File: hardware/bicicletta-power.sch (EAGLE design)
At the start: 24 parts, among them IC1 LM5017, IC2 LM1117-3.3

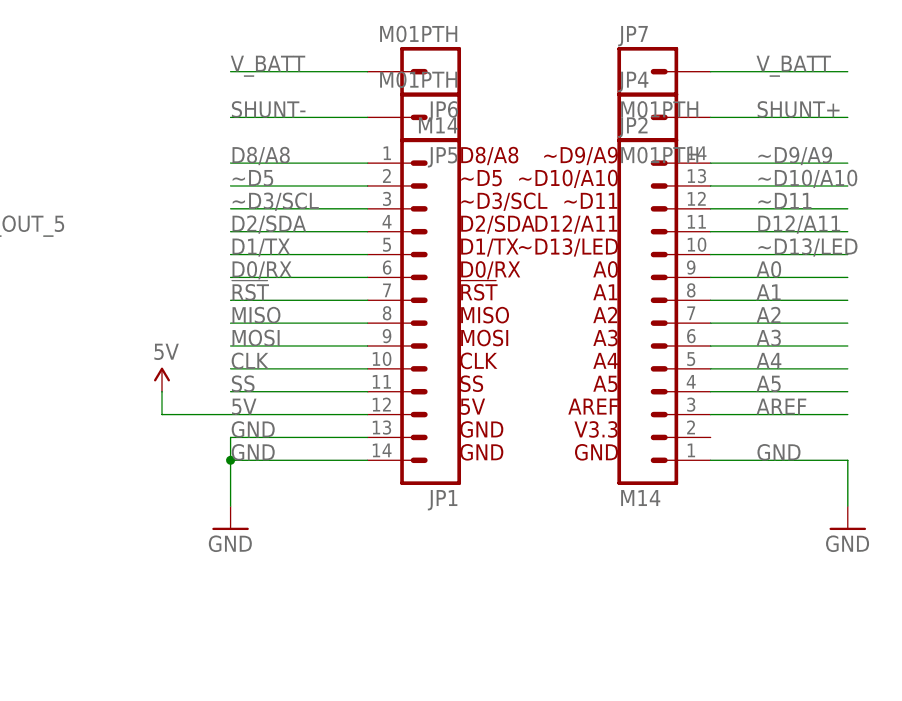
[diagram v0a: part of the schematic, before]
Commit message: Updated to include actual component for the BLEND MICRO
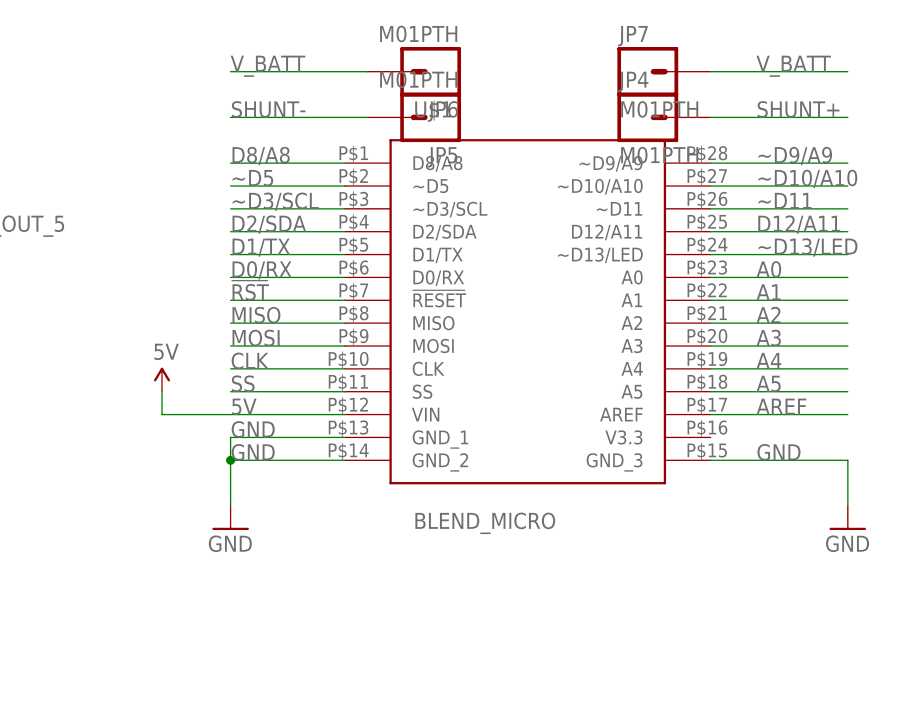
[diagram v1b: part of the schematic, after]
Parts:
- removed JP1, JP2: M14, SparkFun-Connectors:M14
- added U$1: BLEND_MICRO, Railstars:BLEND_MICRO
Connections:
- net !RST: now also U$1.!RESET; no longer JP1.7
- net 5V: now also U$1.VIN; no longer JP1.12
- net A0: now also U$1.A0; no longer JP2.9
- net A1: now also U$1.A1; no longer JP2.8
- net A2: now also U$1.A2; no longer JP2.7
- net A3: now also U$1.A3; no longer JP2.6
- net A4: now also U$1.A4; no longer JP2.5
- net A5: now also U$1.A5; no longer JP2.4
- net AREF: now also U$1.AREF; no longer JP2.3
- net CLK: now also U$1.CLK; no longer JP1.10
- net D0/RX: now also U$1.D0/RX; no longer JP1.6
- net D1/TX: now also U$1.D1/TX; no longer JP1.5
- net D12/A11: now also U$1.D12/A11; no longer JP2.11
- net D2/SDA: now also U$1.D2/SDA; no longer JP1.4
- net D8/A8: now also U$1.D8/A8; no longer JP1.1
- net GND: now also U$1.GND_1, U$1.GND_2, U$1.GND_3; no longer JP1.13, JP1.14, JP2.1
- net MISO: now also U$1.MISO; no longer JP1.8
- net MOSI: now also U$1.MOSI; no longer JP1.9
- net SHUNT-: now also JP5.1
- net SS: now also U$1.SS; no longer JP1.11
- net ~D10/A10: now also U$1.~D10/A10; no longer JP2.13
- net ~D11: now also U$1.~D11; no longer JP2.12
- net ~D13/LED: now also U$1.~D13/LED; no longer JP2.10
- net ~D3/SCL: now also U$1.~D3/SCL; no longer JP1.3
- net ~D5: now also U$1.~D5; no longer JP1.2
- net ~D9/A9: now also U$1.~D9/A9; no longer JP2.14
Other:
- note removed: "!RST"
- note removed: "5V"
- note removed: "A0"
- note removed: "A1"
- note removed: "A2"
- note removed: "A3"
- note removed: "A4"
- note removed: "A5"
- note removed: "AREF"
- note removed: "CLK"
- note removed: "D0/RX"
- note removed: "D1/TX"
- note removed: "D12/A11"
- note removed: "D2/SDA"
- note removed: "D8/A8"
- note removed: "GND"
- note removed: "MISO"
- note removed: "MOSI"
- note removed: "SS"
- note removed: "V3.3"
- note removed: "~D10/A10"
- note removed: "~D11"
- note removed: "~D13/LED"
- note removed: "~D3/SCL"
- note removed: "~D5"
- note removed: "~D9/A9"

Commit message: Rethinking the PCB layout to be more compact.
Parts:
- JP3: device SparkFun-Connectors:M06LONGPADS -> SparkFun-Connectors:M06SIP
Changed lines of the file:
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@@
 <part name="C_R" library="rcl" deviceset="C-US" device="C0603" value="3300pF"/>
 <part name="C_AC" library="rcl" deviceset="C-US" device="C0603" value="100nF"/>
-<part name="JP3" library="SparkFun-Connectors" deviceset="M06" device="LONGPADS"/>
+<part name="JP3" library="SparkFun-Connectors" deviceset="M06" device="SIP"/>
 <part name="JP4" library="SparkFun-Connectors" deviceset="M01" device="PTH"/>
 <part name="JP5" library="SparkFun-Connectors" deviceset="M01" device="PTH"/>

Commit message: Inductor speced out. PCB placement getting closer.
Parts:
- L1: device rcl:L-USL1812 -> Railstars:SRN1060
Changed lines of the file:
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@@
 <part name="R_UV2" library="rcl" deviceset="R-US_" device="M0805" value="125K"/>
 <part name="R_UV1" library="rcl" deviceset="R-US_" device="M0805" value="14K"/>
-<part name="L1" library="rcl" deviceset="L-US" device="L1812" value="100uH"/>
+<part name="L1" library="Railstars" deviceset="SRN1060" device="" value="100uH"/>
 <part name="R_R" library="rcl" deviceset="R-US_" device="M0805" value="2M"/>
 <part name="U$7" library="SparkFun-Aesthetics" deviceset="5V" device=""/>

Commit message: SMall tweaks that add up.
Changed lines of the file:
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@@
 <pinref part="IC1" gate="G$1" pin="GND"/>
 <pinref part="GND1" gate="1" pin="GND"/>
-<wire x1="76.2" y1="109.22" x2="76.2" y2="106.68" width="0.1524" layer="91"/>
 <pinref part="C_IN" gate="G$1" pin="2"/>
-<wire x1="76.2" y1="106.68" x2="76.2" y2="104.14" width="0.1524" layer="91"/>
+<wire x1="76.2" y1="109.22" x2="76.2" y2="104.14" width="0.1524" layer="91"/>
 <wire x1="27.94" y1="127" x2="27.94" y2="109.22" width="0.1524" layer="91"/>
 <wire x1="27.94" y1="109.22" x2="60.96" y2="109.22" width="0.1524" layer="91"/>
@@
 <junction x="60.96" y="109.22"/>
 <pinref part="C_OUT" gate="G$1" pin="2"/>
-<wire x1="76.2" y1="106.68" x2="101.6" y2="106.68" width="0.1524" layer="91"/>
-<wire x1="101.6" y1="106.68" x2="124.46" y2="106.68" width="0.1524" layer="91"/>
-<wire x1="124.46" y1="106.68" x2="132.08" y2="106.68" width="0.1524" layer="91"/>
-<wire x1="132.08" y1="106.68" x2="132.08" y2="119.38" width="0.1524" layer="91"/>
+<wire x1="76.2" y1="109.22" x2="101.6" y2="109.22" width="0.1524" layer="91"/>
+<wire x1="101.6" y1="109.22" x2="124.46" y2="109.22" width="0.1524" layer="91"/>
+<wire x1="124.46" y1="109.22" x2="132.08" y2="109.22" width="0.1524" layer="91"/>
+<wire x1="132.08" y1="109.22" x2="132.08" y2="119.38" width="0.1524" layer="91"/>
 <pinref part="C_VCC" gate="G$1" pin="2"/>
 <wire x1="99.06" y1="124.46" x2="101.6" y2="124.46" width="0.1524" layer="91"/>
-<wire x1="101.6" y1="124.46" x2="101.6" y2="106.68" width="0.1524" layer="91"/>
-<junction x="101.6" y="106.68"/>
+<wire x1="101.6" y1="124.46" x2="101.6" y2="109.22" width="0.1524" layer="91"/>
+<junction x="101.6" y="109.22"/>
 <pinref part="R_FB1" gate="G$1" pin="1"/>
-<wire x1="124.46" y1="114.3" x2="124.46" y2="106.68" width="0.1524" layer="91"/>
-<junction x="124.46" y="106.68"/>
+<wire x1="124.46" y1="114.3" x2="124.46" y2="109.22" width="0.1524" layer="91"/>
+<junction x="124.46" y="109.22"/>
 </segment>
 <segment>

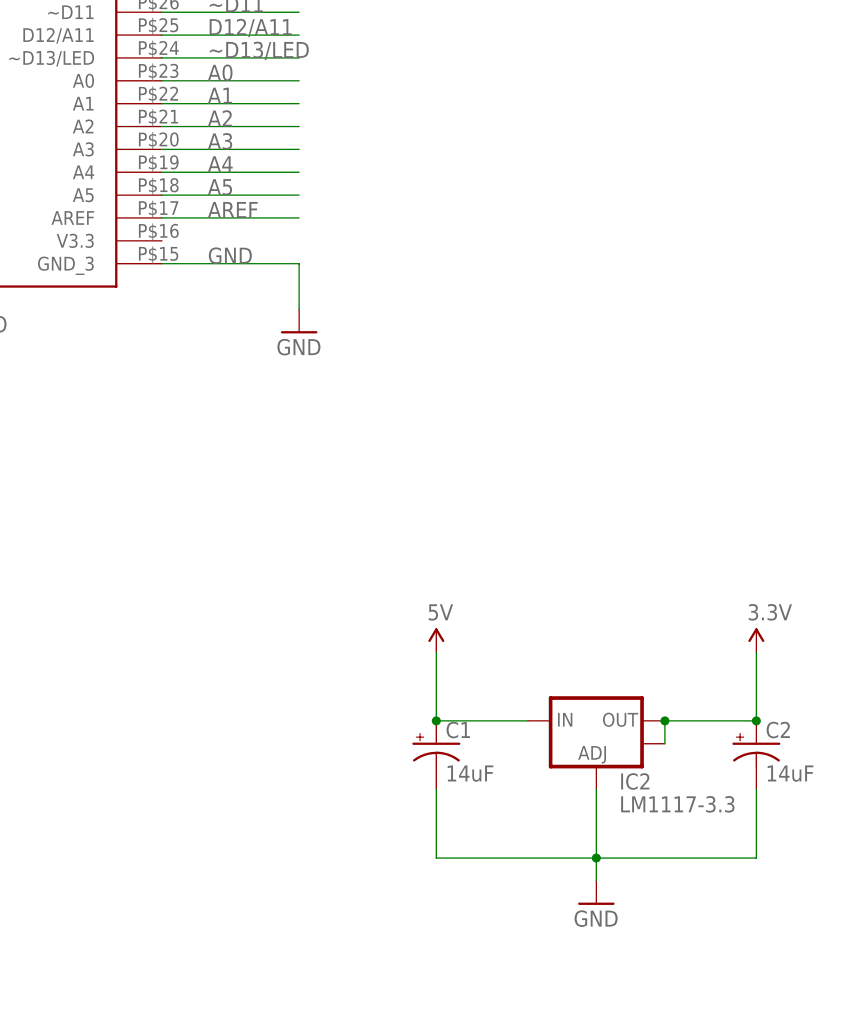
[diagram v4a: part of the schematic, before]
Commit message: Why not use the Blend's 150mA 3.3V regulator?
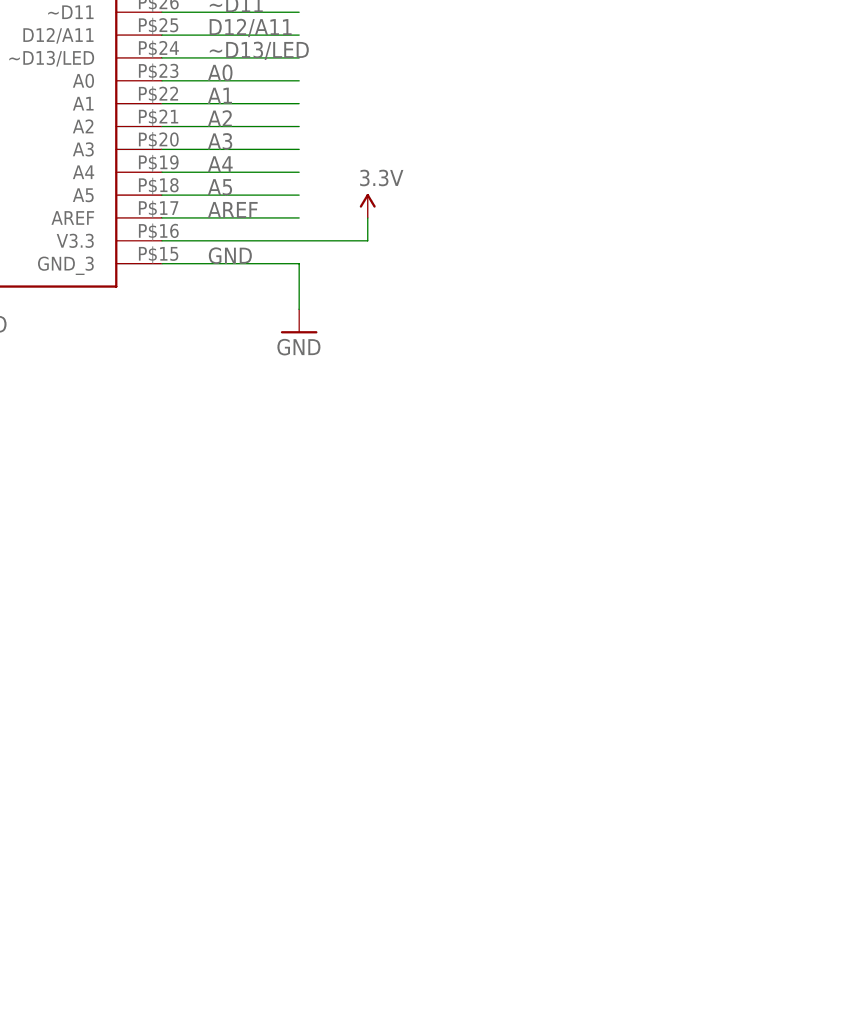
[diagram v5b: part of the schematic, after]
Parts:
- removed C1, C2: 14uF, rcl:CPOL-USUD-5X5,8
- removed IC2: LM1117-3.3, SparkFun-PowerIC:V_REG_LM1117SOT223
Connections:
- net 3.3V: now also U$1.V3.3; no longer C2.+, IC2.OUT, IC2.OUT@1
- net 5V: no longer C1.+, IC2.IN
- net GND: no longer C1.-, C2.-, IC2.ADJ
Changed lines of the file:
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@@
 <part name="R_R" library="rcl" deviceset="R-US_" device="M0805" value="2M"/>
 <part name="U$7" library="SparkFun-Aesthetics" deviceset="5V" device=""/>
-<part name="IC2" library="SparkFun-PowerIC" deviceset="V_REG_LM1117" device="SOT223" value="LM1117-3.3"/>
-<part name="U$8" library="SparkFun-Aesthetics" deviceset="5V" device=""/>
-<part name="GND4" library="SparkFun-Aesthetics" deviceset="GND" device=""/>
 <part name="P+1" library="SparkFun-Aesthetics" deviceset="3.3V" device=""/>
-<part name="C1" library="rcl" deviceset="CPOL-US" device="UD-5X5,8" value="14uF"/>
-<part name="C2" library="rcl" deviceset="CPOL-US" device="UD-5X5,8" value="14uF"/>
 <part name="C_R" library="rcl" deviceset="C-US" device="C0603" value="3300pF"/>
 <part name="C_AC" library="rcl" deviceset="C-US" device="C0603" value="100nF"/>
@@
 <instance part="R_R" gate="G$1" x="104.14" y="129.54"/>
 <instance part="U$7" gate="G$1" x="101.6" y="187.96"/>
-<instance part="IC2" gate="G$1" x="210.82" y="129.54"/>
-<instance part="U$8" gate="G$1" x="193.04" y="137.16"/>
-<instance part="GND4" gate="1" x="210.82" y="109.22"/>
-<instance part="P+1" gate="G$1" x="228.6" y="137.16"/>
-<instance part="C1" gate="G$1" x="193.04" y="127"/>
-<instance part="C2" gate="G$1" x="228.6" y="127"/>
+<instance part="P+1" gate="G$1" x="185.42" y="185.42"/>
 <instance part="C_R" gate="G$1" x="111.76" y="129.54" rot="R90"/>
 <instance part="C_AC" gate="G$1" x="109.22" y="124.46"/>
@@
 </segment>
 <segment>
-<pinref part="IC2" gate="G$1" pin="ADJ"/>
-<pinref part="GND4" gate="1" pin="GND"/>
-<wire x1="210.82" y1="121.92" x2="210.82" y2="114.3" width="0.1524" layer="91"/>
-<pinref part="C2" gate="G$1" pin="-"/>
-<wire x1="210.82" y1="114.3" x2="210.82" y2="111.76" width="0.1524" layer="91"/>
-<wire x1="228.6" y1="121.92" x2="228.6" y2="114.3" width="0.1524" layer="91"/>
-<wire x1="228.6" y1="114.3" x2="210.82" y2="114.3" width="0.1524" layer="91"/>
-<pinref part="C1" gate="G$1" pin="-"/>
-<wire x1="193.04" y1="121.92" x2="193.04" y2="114.3" width="0.1524" layer="91"/>
-<wire x1="193.04" y1="114.3" x2="210.82" y2="114.3" width="0.1524" layer="91"/>
-<junction x="210.82" y="114.3"/>
-</segment>
-<segment>
 <pinref part="JP3" gate="G$1" pin="2"/>
 <wire x1="45.72" y1="195.58" x2="76.2" y2="195.58" width="0.1524" layer="91"/>
@@
 <wire x1="101.6" y1="185.42" x2="101.6" y2="187.96" width="0.1524" layer="91"/>
 <pinref part="U$1" gate="G$1" pin="VIN"/>
-</segment>
-<segment>
-<pinref part="IC2" gate="G$1" pin="IN"/>
-<pinref part="U$8" gate="G$1" pin="5V"/>
-<wire x1="203.2" y1="129.54" x2="193.04" y2="129.54" width="0.1524" layer="91"/>
-<wire x1="193.04" y1="129.54" x2="193.04" y2="137.16" width="0.1524" layer="91"/>
-<pinref part="C1" gate="G$1" pin="+"/>
-<junction x="193.04" y="129.54"/>
 </segment>
 <segment>
@@
 </segment>
 </net>
-<net name="3.3V" class="0">
-<segment>
-<pinref part="IC2" gate="G$1" pin="OUT@1"/>
-<pinref part="IC2" gate="G$1" pin="OUT"/>
-<wire x1="218.44" y1="127" x2="218.44" y2="129.54" width="0.1524" layer="91"/>
-<wire x1="218.44" y1="129.54" x2="228.6" y2="129.54" width="0.1524" layer="91"/>
-<wire x1="228.6" y1="129.54" x2="228.6" y2="137.16" width="0.1524" layer="91"/>
-<pinref part="P+1" gate="G$1" pin="3.3V"/>
-<pinref part="C2" gate="G$1" pin="+"/>
-<junction x="228.6" y="129.54"/>
-<junction x="218.44" y="129.54"/>
-</segment>
-</net>
 <net name="N$4" class="0">
 <segment>
@@
 </segment>
 </net>
+<net name="3.3V" class="0">
+<segment>
+<pinref part="U$1" gate="G$1" pin="V3.3"/>
+<pinref part="P+1" gate="G$1" pin="3.3V"/>
+<wire x1="162.56" y1="182.88" x2="185.42" y2="182.88" width="0.1524" layer="91"/>
+<wire x1="185.42" y1="182.88" x2="185.42" y2="185.42" width="0.1524" layer="91"/>
+</segment>
+</net>

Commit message: There it is. Order that.
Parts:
- removed C_AC: 100nF, rcl:C-USC0603
- removed C_BST: 0.01uF, rcl:C-USC0603
- removed C_R: 3300pF, rcl:C-USC0603
- removed C_VCC: 1uF, rcl:C-USC0603
- removed JP4, JP5, JP6, JP7: M01PTH, SparkFun-Connectors:M01PTH
- removed R_ON: 250K, rcl:R-US_M0805
- removed R_R: 2M, rcl:R-US_M0805
- removed R_UV1: 14K, rcl:R-US_M0805
- removed R_UV2: 125K, rcl:R-US_M0805
- added C_BOOT: 22nF, rcl:C-USC0603
- added C_BYP: 1uF, rcl:C-USC0603
- added C_COMP: 1.8nF, rcl:C-USC0603
- added C_RAMP: 470pF, rcl:C-USC0603
- added C_SS: 1nF, rcl:C-USC0603
- added D1: DFLS1100-7, TI:DFLS1100-7
- added JP1: (no value), SparkFun-Connectors:M06SIP
- added R_COMP: 19K1, rcl:R-US_R0603
- added R_T: 10K7 75V, rcl:R-US_R0603
- C_IN: value 2.2uF -> 1uF; device rcl:C-USC1210K -> rcl:C-USC1206
- C_OUT: value 5.6uF -> 10uF; device rcl:C-USC0603 -> rcl:C-USC0805
- IC1: value LM5017 -> LM5574MT/NOPB; device Railstars:LM5017 -> TI:LM5574MT/NOPB
- L1: value 100uH -> SRN6045-101M; device Railstars:SRN1060 -> TI:SRN6045-101M
- R_FB1: device rcl:R-US_M0805 -> rcl:R-US_R0603
- R_FB2: value 3K -> 3K09; device rcl:R-US_M0805 -> rcl:R-US_R0603
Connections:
- removed net N$4: C_BST.2, IC1.SW, L1.1, R_R.1
- new net N$10: C_BOOT.1, IC1.BST
- new net N$11: C_BOOT.2, D1.K, IC1.PRE, IC1.SW, L1.1
- new net N$5: IC1.RT, R_T.1
- new net N$8: IC1.COMP, R_COMP.1
- net 5V: now also IC1.OUT; no longer C_R.2
- net GND: now also C_BYP.2, C_RAMP.2, C_SS.2, IC1.AGND, IC1.PGND, JP1.2, R_T.2; no longer C_VCC.2, IC1.GND, R_UV1.1
- net N$1: now also C_SS.1, IC1.SS; no longer IC1.RON, R_ON.2
- net N$2: now also C_BYP.1, IC1.VCC; no longer C_AC.2, IC1.FB, R_FB1.2, R_FB2.1
- net N$3: now also C_RAMP.1, IC1.RAMP; no longer IC1.UVLO, R_UV1.2, R_UV2.2
- net N$6: now also C_COMP.2, IC1.FB, R_FB1.2, R_FB2.1; no longer C_AC.1, C_R.1, R_R.2
- net N$7: now also C_COMP.1, R_COMP.2; no longer C_BST.1, IC1.BST
- net N$9: now also D1.A, IC1.IS; no longer C_VCC.1, IC1.V_CC
- net SHUNT+: now also JP1.4; no longer JP4.1
- net SHUNT-: now also JP1.3; no longer JP5.1
- net SPEED_5: now also JP1.5
- net THROTTLE_OUT_5: now also JP1.6
- net V_BATT: now also IC1.VIN, JP1.1; no longer IC1.V_IN, JP6.1, JP7.1, R_ON.1, R_UV2.1
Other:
- note added: "Iout = 500mA"
- note added: "Vout = 5V"
- note removed: "SDR1105-101KL"
- moved on the sheet: C_IN, C_OUT, R_FB1, R_FB2
